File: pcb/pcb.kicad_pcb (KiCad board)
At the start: 2 copper layers, 28 x 59.5 mm, 4 parts, among them J1 CONN_POWER, J2 CONN_EPAPER, J3 CONN_EXT, U1 NodeMCU_1.0_(ESP-12E)

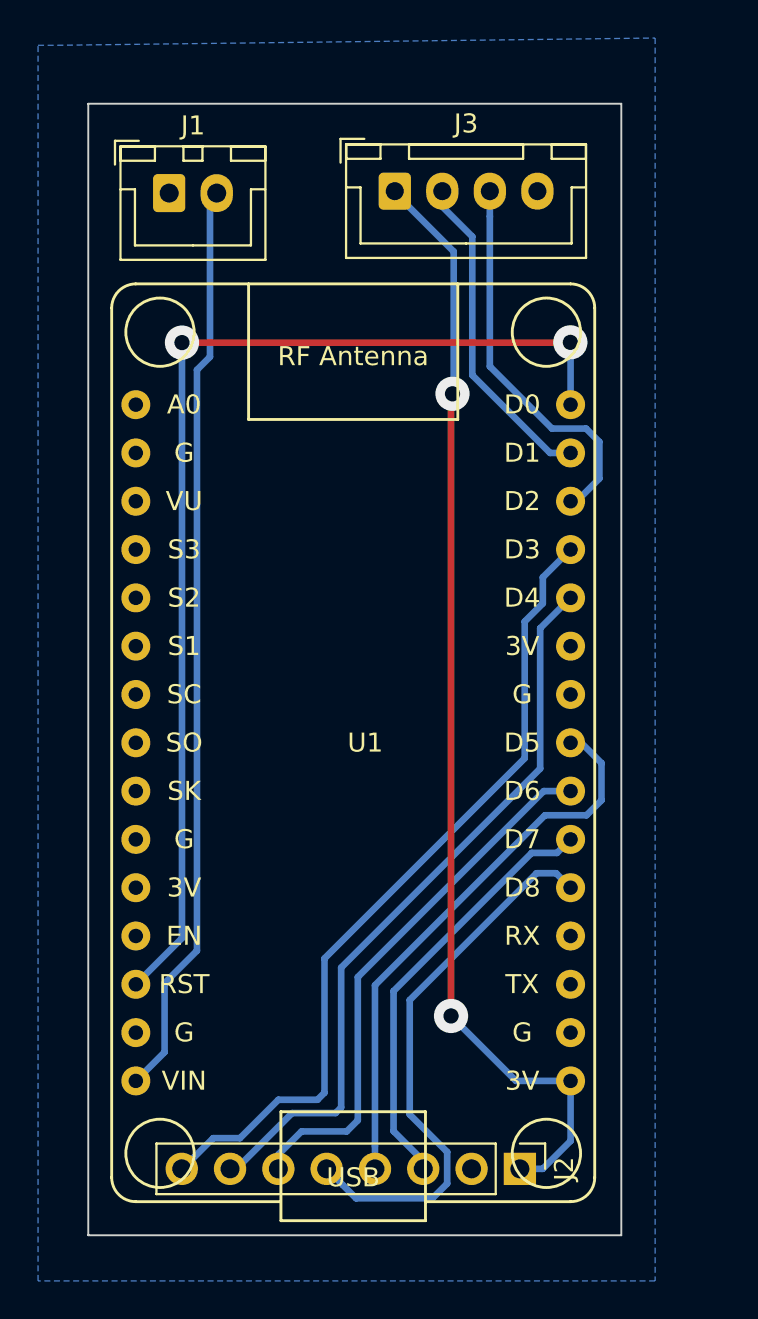
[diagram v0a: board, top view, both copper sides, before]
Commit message: hw: add voltage divider for battery measurement
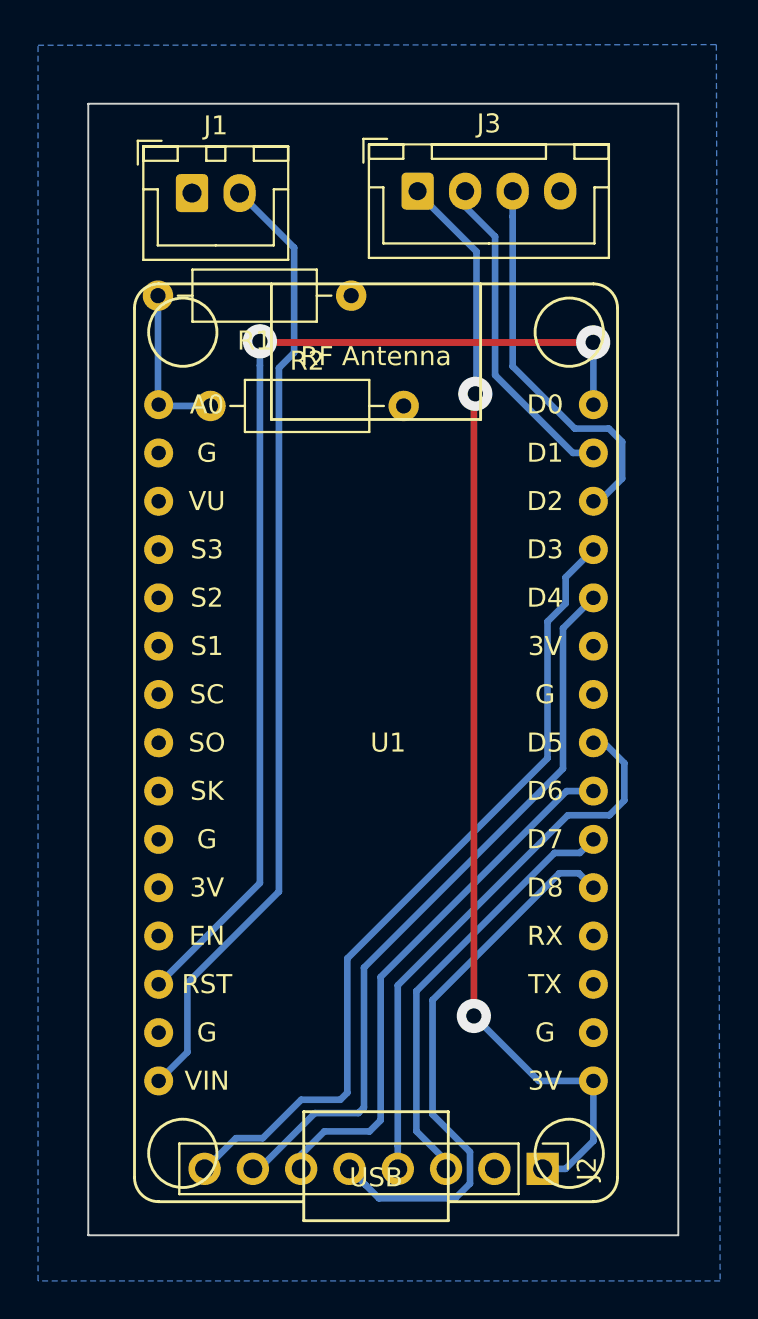
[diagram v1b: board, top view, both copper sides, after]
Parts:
- added R1: 1000, Resistor_THT:R_Axial_DIN0207_L6.3mm_D2.5mm_P10.16mm_Horizontal, F.Cu at (140.0, 86.0)
- added R2: 570, Resistor_THT:R_Axial_DIN0207_L6.3mm_D2.5mm_P10.16mm_Horizontal, F.Cu at (132.6, 91.8)
- moved J3 1.20 mm to (143.5, 80.5)
- moved U1 1.20 mm to (141.3, 110.8)
- moved J1 1.20 mm to (131.6, 80.6)
- moved J2 1.20 mm to (150.1, 131.9)
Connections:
- U1 pad 1: (no net) -> Net-(R1-Pad2)
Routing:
- net Net-(R1-Pad2): track 0.00 -> 8.10 mm
- net +BATT: track 48.4 -> 50.8 mm
- net /RST_WUP: track 58.5 -> 56.8 mm
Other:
- board size 28 x 59.5 mm -> 31 x 59.5 mm

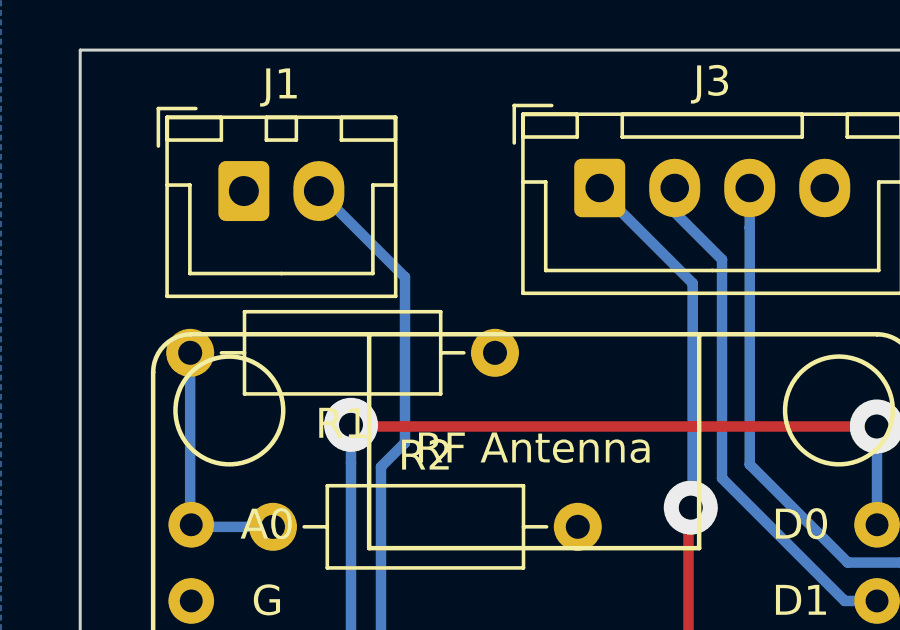
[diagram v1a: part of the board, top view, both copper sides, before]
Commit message: hw: Fix batt not connected
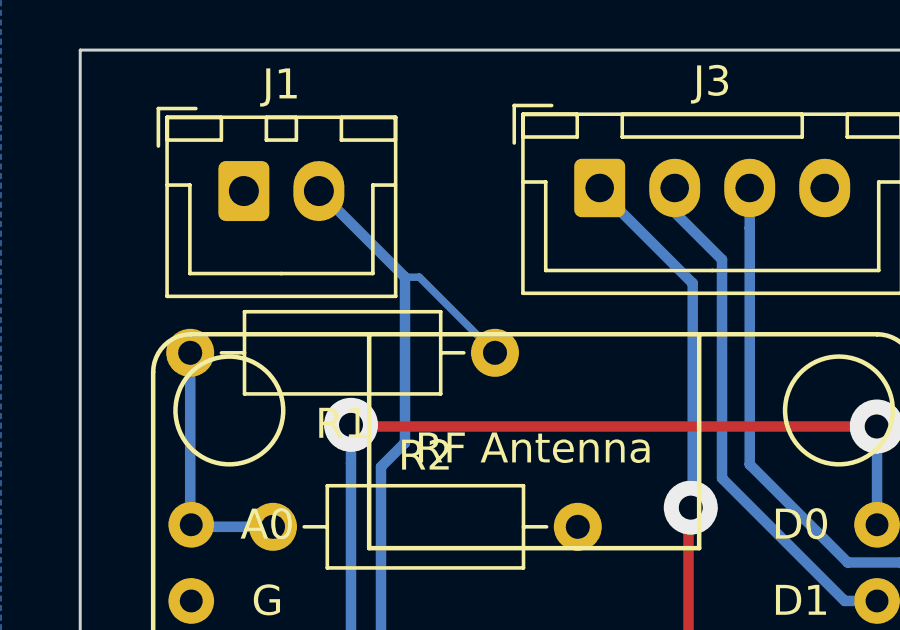
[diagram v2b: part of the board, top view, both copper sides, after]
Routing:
- net +BATT: track 50.8 -> 54.9 mm
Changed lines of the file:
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@@
     (thickness 1.6)
     (drawings 4)
-    (tracks 97)
+    (tracks 99)
     (zones 0)
     (modules 6)
@@
   )
   (setup
-    (last_trace_width 0.35)
+    (last_trace_width 0.25)
     (user_trace_width 0.35)
     (trace_clearance 0.2)
@@
     (add_net GND)
     (add_net "Net-(R1-Pad2)")
-    (add_net "Net-(U1-Pad12)")
-    (add_net "Net-(U1-Pad18)")
-    (add_net "Net-(U1-Pad19)")
-    (add_net "Net-(U1-Pad2)")
-    (add_net "Net-(U1-Pad3)")
-    (add_net "Net-(U1-Pad4)")
-    (add_net "Net-(U1-Pad5)")
-    (add_net "Net-(U1-Pad6)")
-    (add_net "Net-(U1-Pad7)")
-    (add_net "Net-(U1-Pad8)")
-    (add_net "Net-(U1-Pad9)")
   )
   (module Resistor_THT:R_Axial_DIN0207_L6.3mm_D2.5mm_P10.16mm_Horizontal (layer F.Cu)
@@
   (segment (start 136.2 117.3363) (end 136.2 89.8) (width 0.35) (layer B.Cu) (net 2))
   (segment (start 136.2 89.8) (end 137 89) (width 0.35) (layer B.Cu) (net 2))
+  (segment (start 137.4779 83.4779) (end 140 86) (width 0.25) (layer B.Cu) (net 2))
+  (segment (start 137 83.4779) (end 137.4779 83.4779) (width 0.25) (layer B.Cu) (net 2))
   (segment (start 151.2694 131.9149) (end 150.0694 131.9149) (width 0.35) (layer B.Cu) (net 3))
   (segment (start 152.735201 130.449099) (end 151.2694 131.9149) (width 0.35) (layer B.Cu) (net 3))
